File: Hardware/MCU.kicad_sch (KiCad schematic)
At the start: 27 parts, among them J3 SWD, SW2 Reset, SW3 BOOT, U4 STM32L431CBTx, Y1 8M

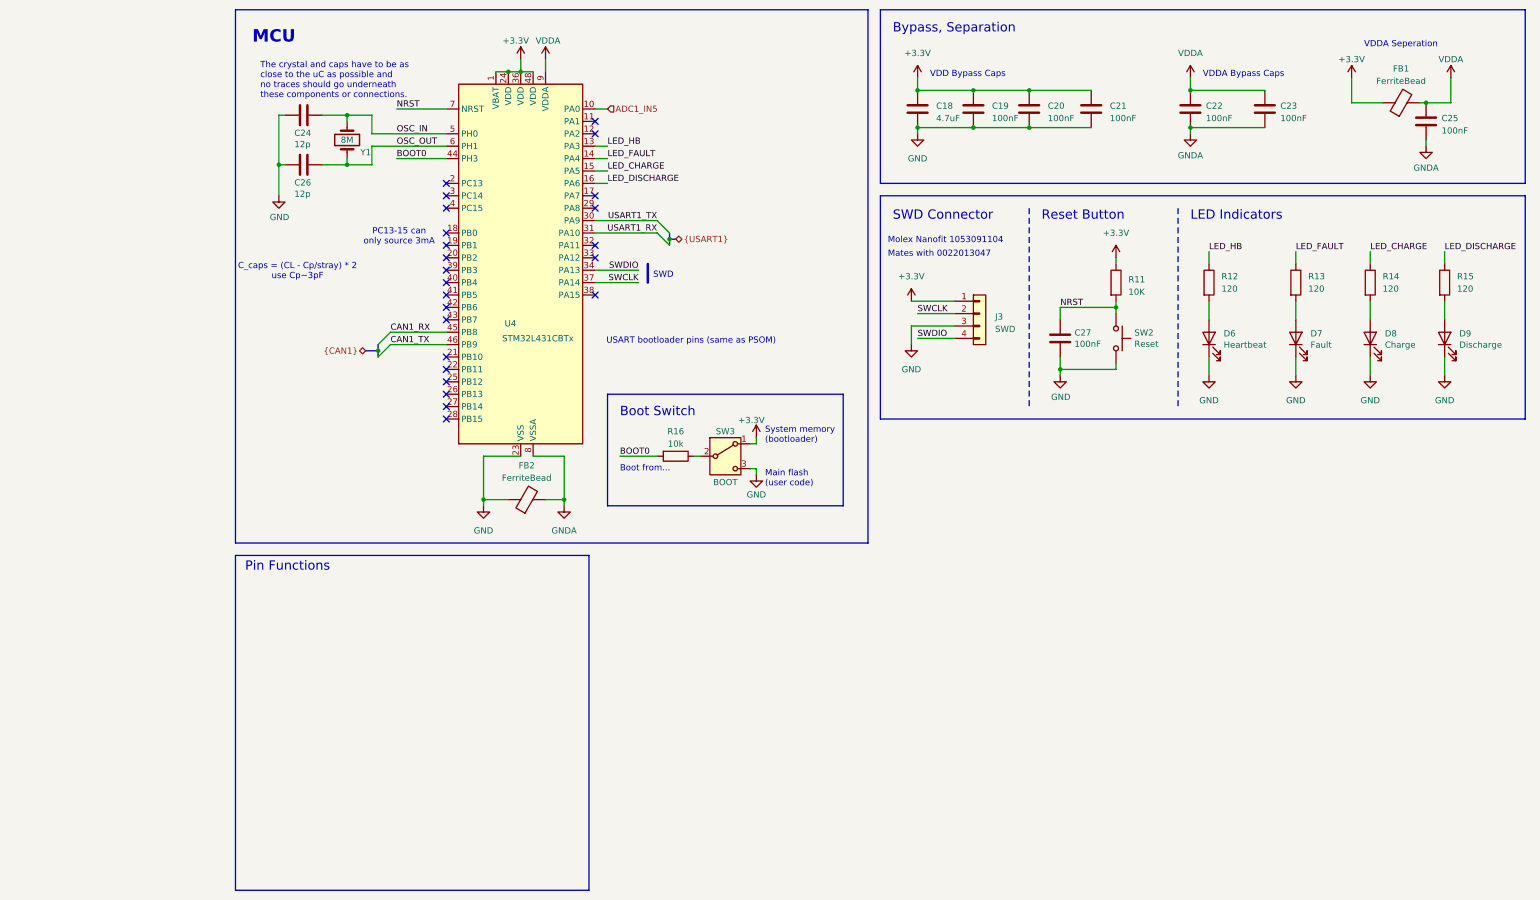
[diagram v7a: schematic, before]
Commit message: 24-5 buck from psom, OR gate for bootload. more sheet organization
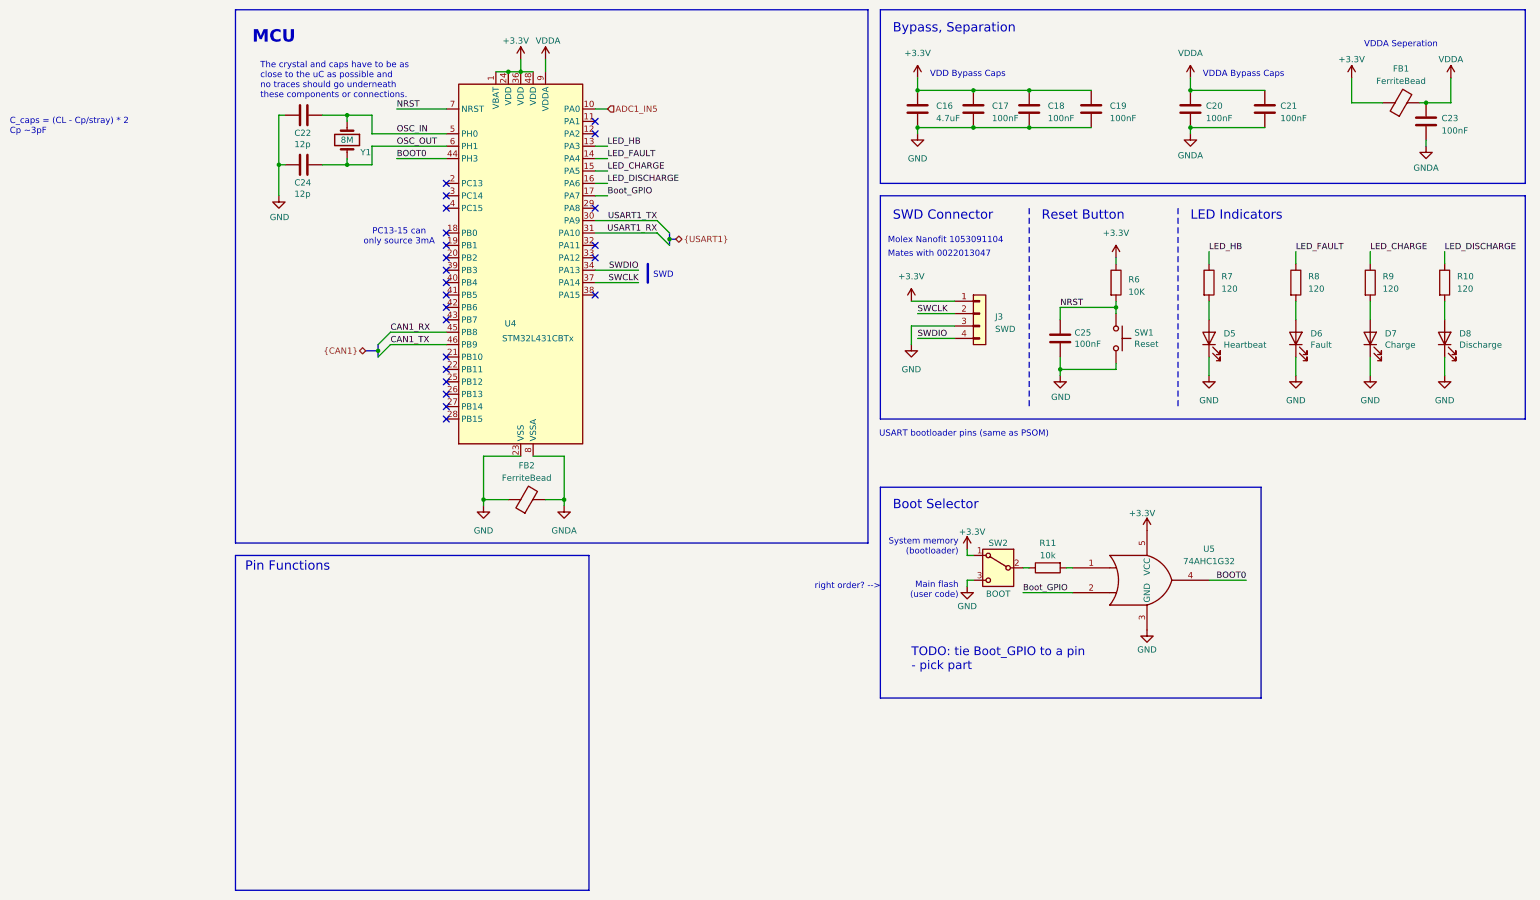
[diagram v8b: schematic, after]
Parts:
- added U5: 74AHC1G32, symbol 74xGxx:74AHC1G32
- renumbered C18 to C16, C19 to C17, C20 to C18, C21 to C19, C22 to C20, C23 to C21, C24 to C22, C25 to C23, C26 to C24, C27 to C25, D6 to D5, D7 to D6, D8 to D7, D9 to D8, R15 to R10, R16 to R11, R11 to R6, R12 to R7, R13 to R8, R14 to R9, SW2 to SW1, SW3 to SW2
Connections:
- net +3.3V: now also U5.5 (VCC)
- net BOOT0: now also U5.4; no longer R11.2
- net GND: now also U5.3 (GND)
- net Boot_GPIO: now reaches U4.17 (PA7)
- net Boot_GPIO: now also U5.2
- new net: R11.2, U5.1
- no-connect marks 24 -> 23
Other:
- note added: "Boot Selector"
- note added: "C_caps = (CL - Cp/stray) * 2 Cp ~3pF"
- note added: "TODO: tie Boot_GPIO to a pin - pick part"
- note added: "right order? -->"
- note removed: "Boot Switch"
- note removed: "Boot from..."
- note removed: "C_caps = (CL - Cp/stray) * 2 use Cp~3pF"
- moved on the sheet: R11, SW2
